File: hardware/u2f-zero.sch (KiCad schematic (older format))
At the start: 16 parts, among them SW1 SW_PUSH

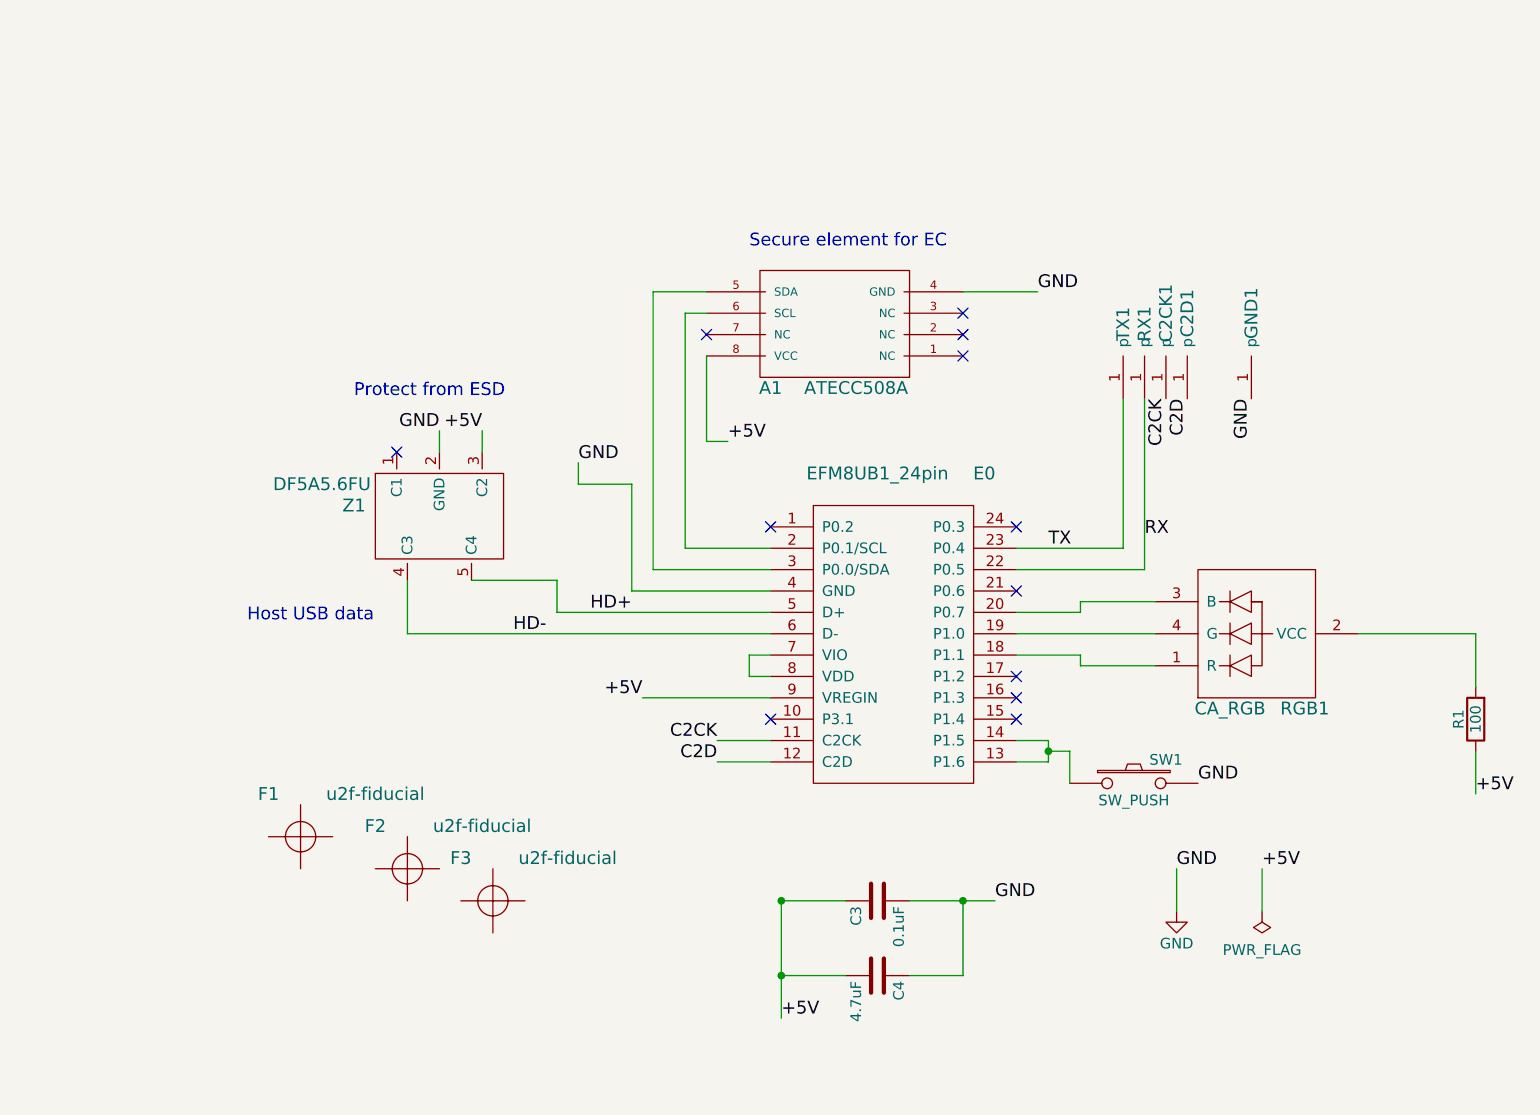
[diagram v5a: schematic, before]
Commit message: add USB-A and USB footprints/symbols.  Add USB-A to layout.
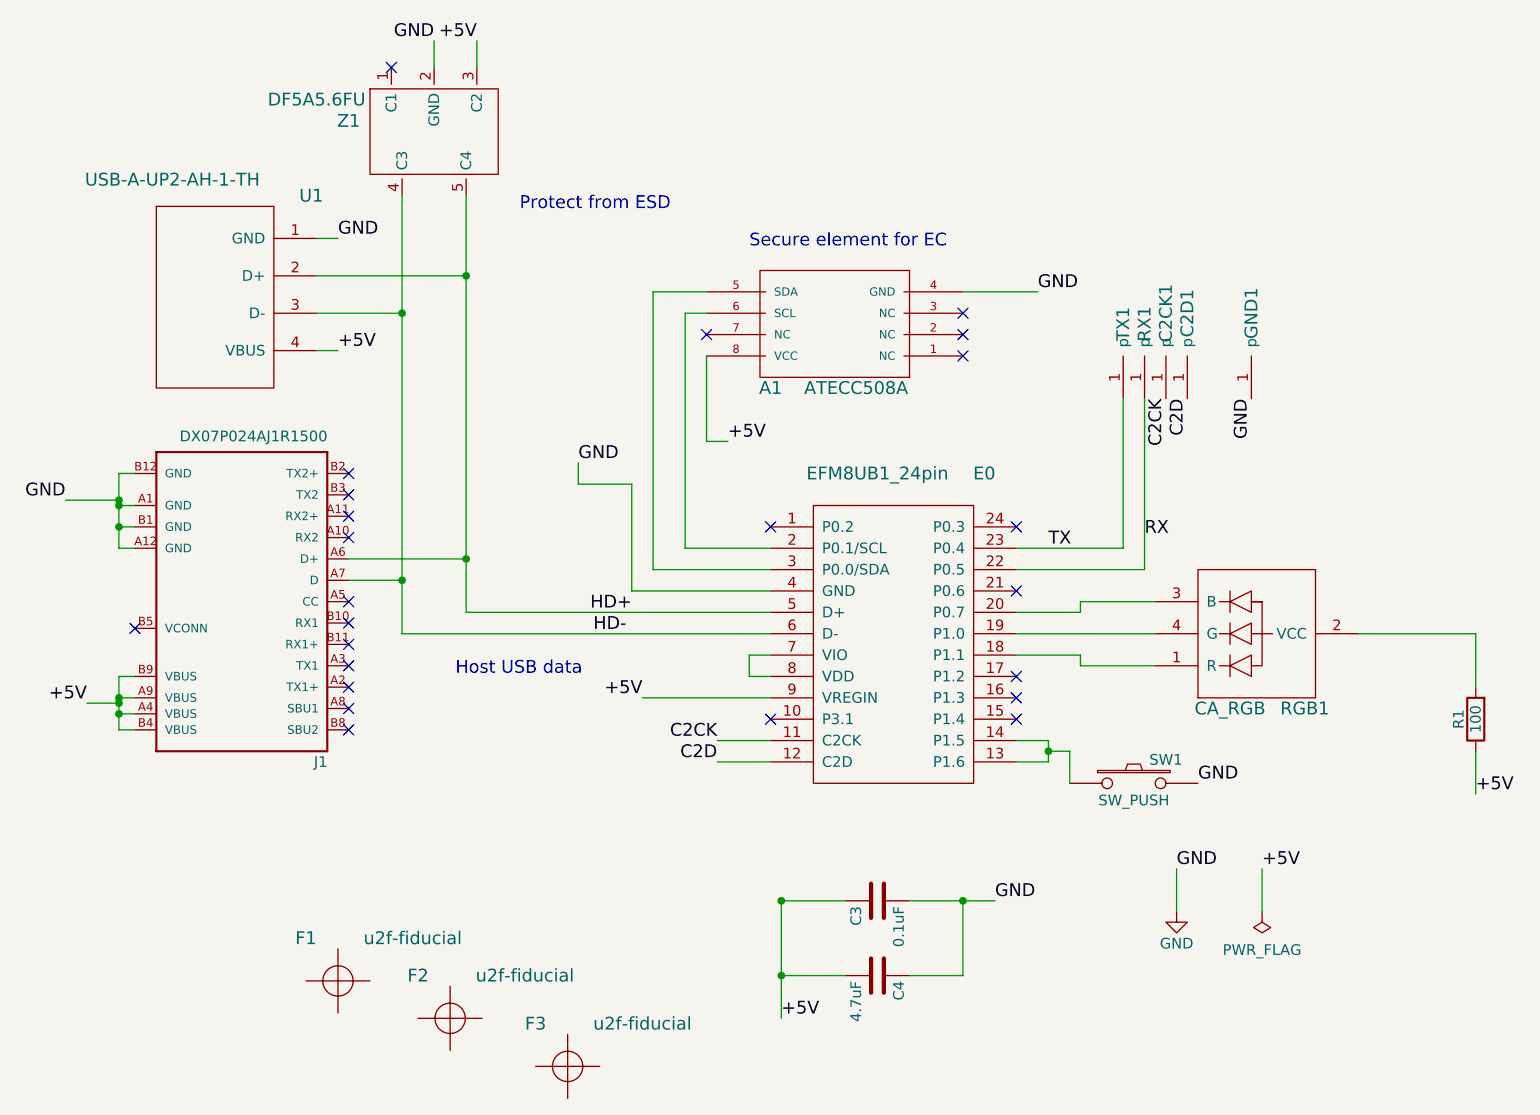
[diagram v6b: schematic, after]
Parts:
- added J1: DX07P024AJ1R1500, footprints:JAE_DX07P024AJ1R1500, symbol DX07P024AJ1R1500
- added U1: USB-A-UP2-AH-1-TH, footprints:usb-A-plug-UP2-AH-1-TH, symbol USB-A-UP2-AH-1-TH
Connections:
- net +5V: now also J1.A4 (VBUS), J1.A9 (VBUS), J1.B4 (VBUS), J1.B9 (VBUS), U1.4 (VBUS)
- net GND: now also J1.A1 (GND), J1.A12 (GND), J1.B1 (GND), J1.B12 (GND), U1.1 (GND)
- net HD+: now also J1.A6 (D+), U1.2 (D+)
- net HD-: now also J1.A7 (D), U1.3 (D-)
- no-connect marks 12 -> 24
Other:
- moved on the sheet: F1, F2, F3, Z1
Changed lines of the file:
@@
 LIBS:discrete
 LIBS:debug
+LIBS:DX07P024AJ1R1500
 LIBS:u2f-zero-cache
 EELAYER 25 0
@@
 L DF5A5.6JE Z1
 U 1 1 56857EAF
-P 3250 3950
-F 0 "Z1" H 2850 4000 60  0000 C CNN
-F 1 "DF5A5.6FU" H 2700 4100 60  0000 C CNN
-F 2 "TO_SOT_Packages_SMD:SOT-353_SC-70-5" H 3250 3950 60  0001 C CNN
-F 3 "https://toshiba.semicon-storage.com/info/docget.jsp?did=22252&prodName=DF5A5.6FU" H 3250 3950 60  0001 C CNN
-F 4 "Toshiba Semiconductor and Storage" H 3250 3950 60  0001 C CNN "MFG Name"
-F 5 "DF5A5.6FUTE85LF" H 3250 3950 60  0001 C CNN "MFG Part Num"
-F 6 "DF5A5.6FUTE85LFCT-ND" H 3250 3950 60  0001 C CNN "Distributer PN"
-F 7 "https://www.digikey.com/product-detail/en/toshiba-semiconductor-and-storage/DF5A5.6FUTE85LF/DF5A5.6FUTE85LFCT-ND/4304119" H 3250 3950 60  0001 C CNN "Distributer Link"
-	1    3250 3950
+P 3225 2150
+F 0 "Z1" H 2825 2200 60  0000 C CNN
+F 1 "DF5A5.6FU" H 2675 2300 60  0000 C CNN
+F 2 "TO_SOT_Packages_SMD:SOT-353_SC-70-5" H 3225 2150 60  0001 C CNN
+F 3 "https://toshiba.semicon-storage.com/info/docget.jsp?did=22252&prodName=DF5A5.6FU" H 3225 2150 60  0001 C CNN
+F 4 "Toshiba Semiconductor and Storage" H 3225 2150 60  0001 C CNN "MFG Name"
+F 5 "DF5A5.6FUTE85LF" H 3225 2150 60  0001 C CNN "MFG Part Num"
+F 6 "DF5A5.6FUTE85LFCT-ND" H 3225 2150 60  0001 C CNN "Distributer PN"
+F 7 "https://www.digikey.com/product-detail/en/toshiba-semiconductor-and-storage/DF5A5.6FUTE85LF/DF5A5.6FUTE85LFCT-ND/4304119" H 3225 2150 60  0001 C CNN "Distributer Link"
+	1    3225 2150
 	1    0    0    -1
 $EndComp
@@
 Text Label 4850 6300 0    60   ~ 0
 +5V
-Text Label 3450 3550 2    60   ~ 0
-+5V
-Text Label 3250 3550 2    60   ~ 0
-GND
-Text Label 3750 4500 2    60   ~ 0
+Text Label 3425 1725 2    60   ~ 0
++5V
+Text Label 3225 1725 2    60   ~ 0
+GND
+Text Label 4125 4500 2    60   ~ 0
 HD-
 Text Label 4150 4400 2    60   ~ 0
@@
 	-1   0    0    1
 $EndComp
-Text Notes 2850 3400 0    60   ~ 0
+Text Notes 3625 2525 0    60   ~ 0
 Protect from ESD
-Text Notes 2350 4450 0    60   ~ 0
+Text Notes 3325 4700 0    60   ~ 0
 Host USB data
 Text Notes 4700 2700 0    60   ~ 0
@@
 	1    0    0    -1
 $EndComp
-NoConn ~ 3050 3650
 Text Label 6650 3400 3    60   ~ 0
 C2CK
@@
 	6700 5600 6700 5800
 Wire Wire Line
-	3100 4250 3100 4500
-Wire Wire Line
-	3250 3650 3250 3550
-Wire Wire Line
-	3450 3650 3450 3550
-Wire Wire Line
 	6450 3400 6450 4100
 Wire Wire Line
@@
 	4800 5000 4550 5000
 Wire Wire Line
-	4800 4400 3800 4400
-Wire Wire Line
-	3800 4400 3800 4250
-Wire Wire Line
-	3800 4250 3400 4250
-Wire Wire Line
-	3100 4500 4800 4500
+	3375 4400 4800 4400
+Wire Wire Line
+	3075 4500 4800 4500
 Wire Wire Line
 	6600 4350 6250 4350
@@
 L u2f-fiducial F1
 U 1 1 571C39BB
-P 2600 5450
-F 0 "F1" H 2450 5650 60  0000 C CNN
-F 1 "u2f-fiducial" H 2950 5650 60  0000 C CNN
-F 2 "footprints:u2f-fiducial" H 2600 5450 60  0001 C CNN
-F 3 "" H 2600 5450 60  0000 C CNN
-	1    2600 5450
+P 2775 6125
+F 0 "F1" H 2625 6325 60  0000 C CNN
+F 1 "u2f-fiducial" H 3125 6325 60  0000 C CNN
+F 2 "footprints:u2f-fiducial" H 2775 6125 60  0001 C CNN
+F 3 "" H 2775 6125 60  0000 C CNN
+	1    2775 6125
 	1    0    0    -1
 $EndComp
@@
 L u2f-fiducial F2
 U 1 1 571C3A1E
-P 3100 5600
-F 0 "F2" H 2950 5800 60  0000 C CNN
-F 1 "u2f-fiducial" H 3450 5800 60  0000 C CNN
-F 2 "footprints:u2f-fiducial" H 3100 5600 60  0001 C CNN
-F 3 "" H 3100 5600 60  0000 C CNN
-	1    3100 5600
+P 3300 6300
+F 0 "F2" H 3150 6500 60  0000 C CNN
+F 1 "u2f-fiducial" H 3650 6500 60  0000 C CNN
+F 2 "footprints:u2f-fiducial" H 3300 6300 60  0001 C CNN
+F 3 "" H 3300 6300 60  0000 C CNN
+	1    3300 6300
 	1    0    0    -1
 $EndComp
@@
 L u2f-fiducial F3
 U 1 1 571C3A85
-P 3500 5750
-F 0 "F3" H 3350 5950 60  0000 C CNN
-F 1 "u2f-fiducial" H 3850 5950 60  0000 C CNN
-F 2 "footprints:u2f-fiducial" H 3500 5750 60  0001 C CNN
-F 3 "" H 3500 5750 60  0000 C CNN
-	1    3500 5750
-	1    0    0    -1
-$EndComp
+P 3850 6525
+F 0 "F3" H 3700 6725 60  0000 C CNN
+F 1 "u2f-fiducial" H 4200 6725 60  0000 C CNN
+F 2 "footprints:u2f-fiducial" H 3850 6525 60  0001 C CNN
+F 3 "" H 3850 6525 60  0000 C CNN
+	1    3850 6525
+	1    0    0    -1
+$EndComp
+$Comp
+L DX07P024AJ1R1500 J1
+U 1 1 5AE12773
+P 2325 4350
+F 0 "J1" H 1924 5071 50  0000 L BNN
+F 1 "DX07P024AJ1R1500" H 1924 3547 50  0000 L BNN
+F 2 "footprints:JAE_DX07P024AJ1R1500" H 2325 4350 50  0001 L BNN
+F 3 "Good" H 2325 4350 50  0001 L BNN
+F 4 "DX07P024AJ1R1500" H 2325 4350 50  0001 L BNN "Field4"
+F 5 "1.37 USD" H 2325 4350 50  0001 L BNN "Field5"
+F 6 "JAE Electronics" H 2325 4350 50  0001 L BNN "Field6"
+F 7 "None" H 2325 4350 50  0001 L BNN "Field7"
+F 8 "Cut Tape - Usb Type c Slim Plug" H 2325 4350 50  0001 L BNN "Field8"
+	1    2325 4350
+	-1   0    0    1
+$EndComp
+Wire Wire Line
+	3425 1850 3425 1725
+Wire Wire Line
+	3225 1725 3225 1850
+Wire Wire Line
+	3375 2450 3375 4400
+Wire Wire Line
+	3075 2450 3075 4500
+Wire Wire Line
+	2825 4150 3375 4150
+Connection ~ 3375 4150
+Wire Wire Line
+	2825 4250 3075 4250
+Connection ~ 3075 4250
+NoConn ~ 2825 3750
+NoConn ~ 2825 3850
+NoConn ~ 2825 3950
+NoConn ~ 2825 4050
+NoConn ~ 2825 4350
+NoConn ~ 2825 4450
+NoConn ~ 2825 4550
+NoConn ~ 2825 4650
+NoConn ~ 2825 4750
+NoConn ~ 2825 4850
+NoConn ~ 2825 4950
+NoConn ~ 3025 1850
+Text Label 1600 4825 2    60   ~ 0
++5V
+Text Label 1500 3875 2    60   ~ 0
+GND
+Wire Wire Line
+	1750 4100 1750 3750
+Wire Wire Line
+	1750 3750 1825 3750
+Wire Wire Line
+	1825 3900 1750 3900
+Connection ~ 1750 3900
+Wire Wire Line
+	1825 4000 1750 4000
+Connection ~ 1750 4000
+Wire Wire Line
+	1750 4100 1825 4100
+Wire Wire Line
+	1500 3875 1750 3875
+Connection ~ 1750 3875
+Wire Wire Line
+	1825 4700 1750 4700
+Wire Wire Line
+	1750 4700 1750 4950
+Wire Wire Line
+	1750 4950 1825 4950
+Wire Wire Line
+	1825 4875 1750 4875
+Connection ~ 1750 4875
+Wire Wire Line
+	1825 4800 1750 4800
+Connection ~ 1750 4800
+Wire Wire Line
+	1600 4825 1750 4825
+Connection ~ 1750 4825
+NoConn ~ 1825 4475
+$Comp
+L USB-A-UP2-AH-1-TH U1
+U 1 1 5AE141F4
+P 2275 2300
+F 0 "U1" H 2650 2150 60  0000 C CNN
+F 1 "USB-A-UP2-AH-1-TH" H 2000 2225 60  0000 C CNN
+F 2 "footprints:usb-A-plug-UP2-AH-1-TH" H 2275 2300 60  0001 C CNN
+F 3 "" H 2275 2300 60  0001 C CNN
+	1    2275 2300
+	1    0    0    -1
+$EndComp
+Wire Wire Line
+	2675 2825 3375 2825
+Connection ~ 3375 2825
+Wire Wire Line
+	2675 3000 3075 3000
+Connection ~ 3075 3000
+Text Label 2775 3175 0    60   ~ 0
++5V
+Text Label 2775 2650 0    60   ~ 0
+GND
+Wire Wire Line
+	2775 2650 2675 2650
+Wire Wire Line
+	2775 3175 2675 3175
 $EndSCHEMATC
